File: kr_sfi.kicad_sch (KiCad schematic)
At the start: 85 parts, among them U42 NTS0102_TSSOP, U43 TLK10232CTR, Y2 Oscillator_156.25MHz_SG3225EEN

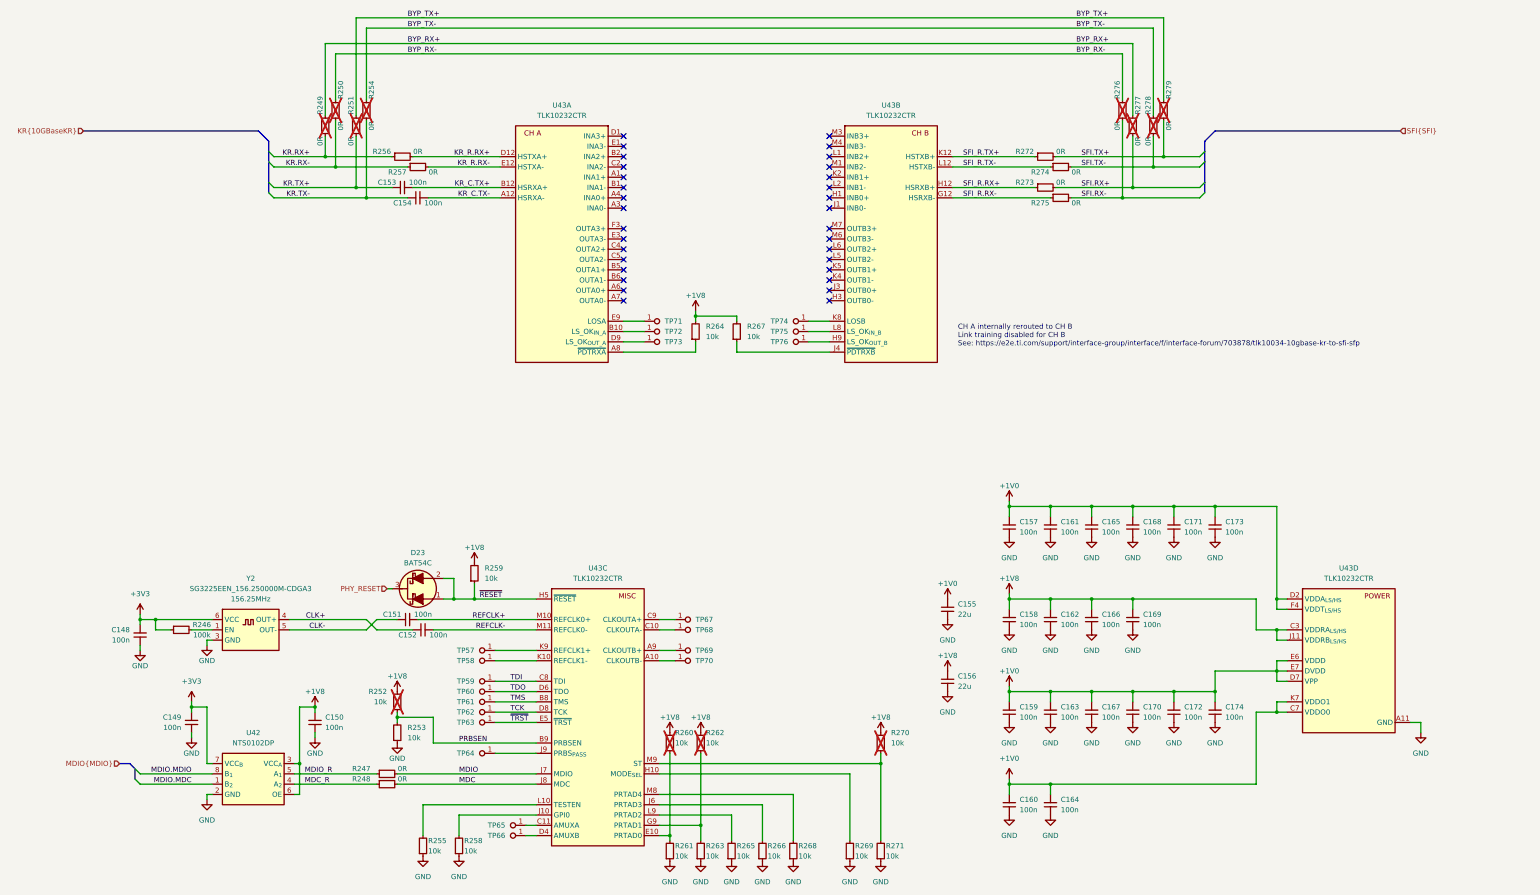
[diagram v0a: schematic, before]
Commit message: [#70030] Routed PCIe
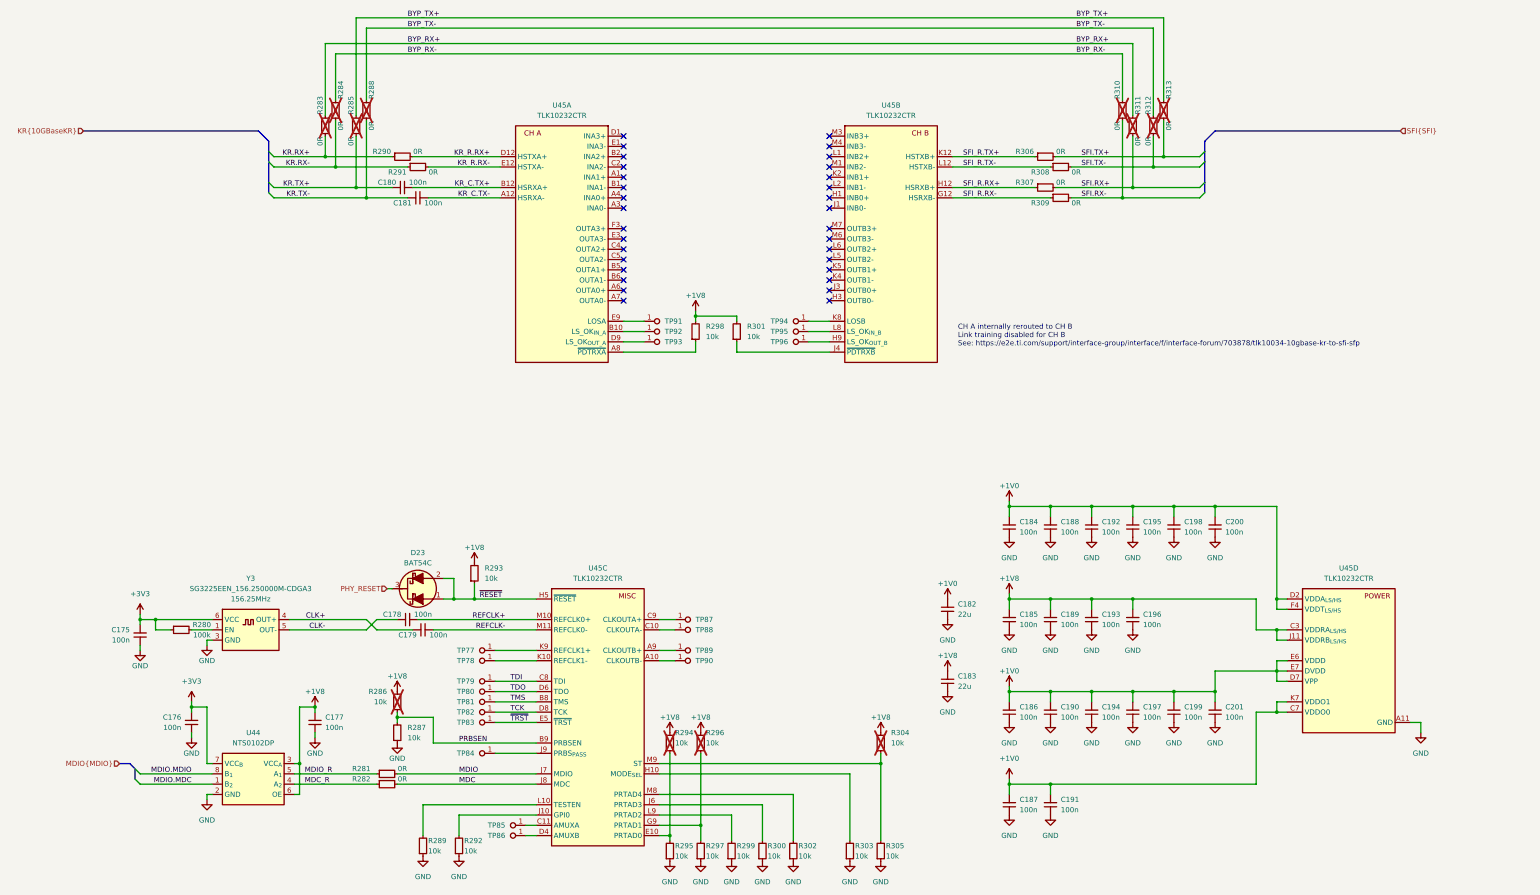
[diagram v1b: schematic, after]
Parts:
- renumbered C148 to C175, C149 to C176, C150 to C177, C151 to C178, C152 to C179, C153 to C180, C154 to C181, C155 to C182, C156 to C183, C157 to C184, C158 to C185, C159 to C186, C160 to C187, C161 to C188, C162 to C189, C163 to C190, C164 to C191, C165 to C192, C166 to C193, C167 to C194, C168 to C195, C169 to C196, C170 to C197, C171 to C198, C172 to C199, C173 to C200, C174 to C201, R246 to R280, R247 to R281, R248 to R282, R249 to R283, R250 to R284, R251 to R285, R252 to R286, R253 to R287, R254 to R288, R255 to R289, R256 to R290, R257 to R291, R258 to R292, R259 to R293, R260 to R294, R261 to R295, R262 to R296, R263 to R297, R264 to R298, R265 to R299, R266 to R300, R267 to R301, R268 to R302, R269 to R303, R270 to R304, R271 to R305, R272 to R306, R273 to R307, R274 to R308, R275 to R309, R276 to R310, R277 to R311, R278 to R312, R279 to R313, TP57 to TP77, TP58 to TP78, TP59 to TP79, TP60 to TP80, TP61 to TP81, TP62 to TP82, TP63 to TP83, TP64 to TP84, TP65 to TP85, TP66 to TP86, TP67 to TP87, TP68 to TP88, TP69 to TP89, TP70 to TP90, TP71 to TP91, TP72 to TP92, TP73 to TP93, TP74 to TP94, TP75 to TP95, TP76 to TP96, U42 to U44, U43 to U45, Y2 to Y3
